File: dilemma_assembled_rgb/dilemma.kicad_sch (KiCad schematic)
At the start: 149 parts, among them J1 USB_C_Receptacle_USB2.0, J102 Serial, J105 Conn_01x04_Female, J113 Cirque, J2 Conn_01x03_Female, J5 Conn_01x02, SW1 SW_Push, SW101 SW_Push, SW102 SW_Push, SW103 SW_Push, SW104 SW_Push, SW105 SW_Push, SW106 SW_Push, SW107 SW_Push, SW108 SW_Push, SW109 SW_Push, SW110 SW_SPST, SW112 SW_Push, SW113 SW_Push, SW114 SW_Push, SW115 SW_Push, SW116 SW_Push, SW117 SW_Push, SW118 SW_Push, SW119 SW_Push, SW2 SW_Push, SW3001 SW_Push, SW3002 RotaryEncoder_Switch, U1 RP2040, U2 GD25Q80CEIGR, U3 XC6210B332MR-G, U4 USBLC6-2P6, Y1 Crystal_GND24

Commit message: edge cuts
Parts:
- D10, D11, D12, D13, D14, D15, D16, D17, D18, D19, D20, D21, D22, D23, D24, D25, D26, D27, D28, D29, D3, D4, D5, D6, D7, D8, D9: footprint 0xB2_drawings:LED_SK6805-EC15_1.5x1.5mm_P0.6mm_handsolder(1) -> 0xB2_drawings:LED_SK6805-EC15_hole
- D101, D102, D103, D104, D105, D106, D107, D108, D109, D110, D111, D112, D113, D114, D115, D116, D117, D3001: footprint local-libraries:D_1206_handsolder_reversible -> local-libraries:D_1206_handsolder_reversible_hole

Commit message: holes
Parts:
- H101, H102, H104: footprint local-libraries:MountingHole_3mm_Pad_Via -> local-libraries:MountingHole_3mm_Pad_hole
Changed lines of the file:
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@@
       (effects (font (size 1.27 1.27)) (justify left))
     )
-    (property "Footprint" "local-libraries:MountingHole_3mm_Pad_Via" (id 2) (at 184.15 176.53 0)
+    (property "Footprint" "local-libraries:MountingHole_3mm_Pad_hole" (id 2) (at 184.15 176.53 0)
       (effects (font (size 1.27 1.27)) hide)
     )
@@
       (effects (font (size 1.27 1.27)) (justify left))
     )
-    (property "Footprint" "local-libraries:MountingHole_3mm_Pad_Via" (id 2) (at 190.5 176.53 0)
+    (property "Footprint" "local-libraries:MountingHole_3mm_Pad_hole" (id 2) (at 190.5 176.53 0)
       (effects (font (size 1.27 1.27)) hide)
     )
@@
       (effects (font (size 1.27 1.27)) (justify left))
     )
-    (property "Footprint" "local-libraries:MountingHole_3mm_Pad_Via" (id 2) (at 209.55 176.53 0)
+    (property "Footprint" "local-libraries:MountingHole_3mm_Pad_hole" (id 2) (at 209.55 176.53 0)
       (effects (font (size 1.27 1.27)) hide)
     )
@@
     )
     (path "/2f4248fc-bac1-4746-8fce-b7d7e338527c"
-      (reference "H101") (unit 1) (value "M4") (footprint "local-libraries:MountingHole_3mm_Pad_Via")
+      (reference "H101") (unit 1) (value "M4") (footprint "local-libraries:MountingHole_3mm_Pad_hole")
     )
     (path "/9cb3ab70-f859-494a-87ac-434fbc66c33e"
-      (reference "H102") (unit 1) (value "M4") (footprint "local-libraries:MountingHole_3mm_Pad_Via")
+      (reference "H102") (unit 1) (value "M4") (footprint "local-libraries:MountingHole_3mm_Pad_hole")
     )
     (path "/6e8fbc4a-2a66-4de2-9627-0a21b2e2f627"
@@
     )
     (path "/b3d2b3b2-eee3-4354-96ae-35ebc3a7e3fd"
-      (reference "H104") (unit 1) (value "M4") (footprint "local-libraries:MountingHole_3mm_Pad_Via")
+      (reference "H104") (unit 1) (value "M4") (footprint "local-libraries:MountingHole_3mm_Pad_hole")
     )
     (path "/f149694e-4336-45f7-8a0b-aed91118ad18"

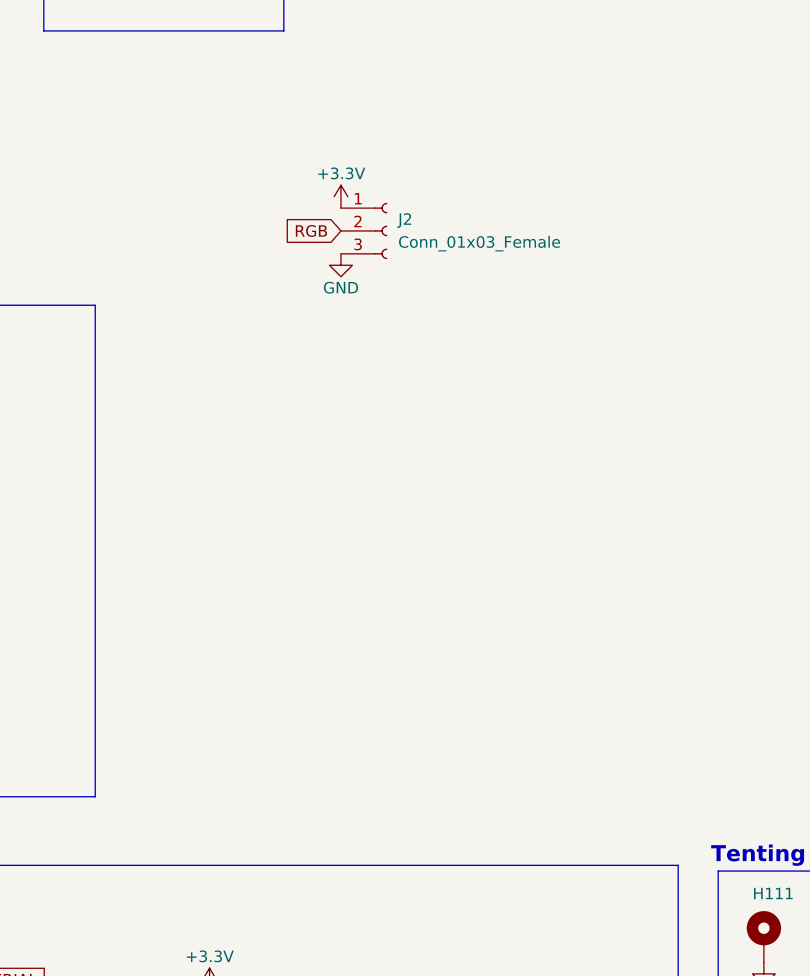
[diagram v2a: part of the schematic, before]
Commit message: switch rgb to smd connectors
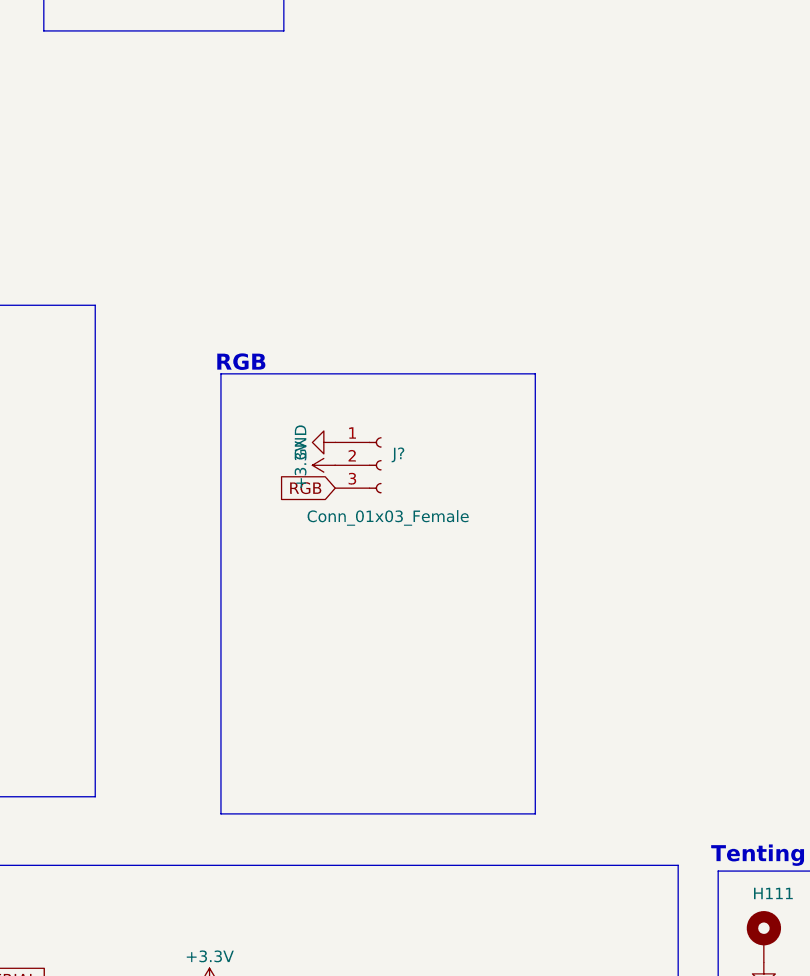
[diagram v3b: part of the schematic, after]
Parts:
- removed J2: Conn_01x03_Female, Connector_PinHeader_2.54mm:PinHeader_1x03_P2.54mm_Vertical, symbol Connector:Conn_01x03_Female
- added J?: Conn_01x03_Female, local-libraries:PinHeader_1x03_P2.54mm_Vertical_smd, symbol Connector:Conn_01x03_Female
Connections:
- net +3V3: now also J?.2 (Pin_2)
- net GND: now also J?.1 (Pin_1)
- net RGB: now also J?.3 (Pin_3)
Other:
- note added: "RGB"
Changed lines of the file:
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@@
     (stroke (width 0) (type default) (color 0 0 0 0))
   )
+  (polyline (pts (xy 293.37 111.76) (xy 328.295 111.76))
+    (stroke (width 0) (type default) (color 0 0 0 0))
+  )
   (wire (pts (xy 267.97 137.16) (xy 256.54 137.16))
     (stroke (width 0) (type default) (color 0 0 0 0))
@@
     (stroke (width 0) (type default) (color 0 0 0 0))
   )
+  (polyline (pts (xy 328.295 111.76) (xy 328.295 160.655))
+    (stroke (width 0) (type default) (color 0 0 0 0))
+  )
   (wire (pts (xy 139.7 175.26) (xy 148.59 175.26))
     (stroke (width 0) (type default) (color 0 0 0 0))
@@
     (stroke (width 0) (type default) (color 0 0 0 0))
   )
+  (polyline (pts (xy 328.295 160.655) (xy 293.37 160.655))
+    (stroke (width 0) (type default) (color 0 0 0 0))
+  )
   (wire (pts (xy 33.02 215.9) (xy 44.45 215.9))
     (stroke (width 0) (type default) (color 0 0 0 0))
@@
     (stroke (width 0) (type default) (color 0 0 0 0))
   )
+  (polyline (pts (xy 293.37 111.76) (xy 293.37 160.655))
+    (stroke (width 0) (type default) (color 0 0 0 0))
+  )
   (wire (pts (xy 111.76 81.28) (xy 116.84 81.28))
     (stroke (width 0) (type default) (color 0 0 0 0))
@@
     (effects (font (size 1.778 1.778) (thickness 0.3556) bold) (justify left bottom))
   )
+  (text "RGB" (at 292.735 111.76 0)
+    (effects (font (size 1.778 1.778) (thickness 0.3556) bold) (justify left bottom))
+  )
   (text "MCU" (at 86.36 20.32 0)
     (effects (font (size 1.778 1.778) (thickness 0.3556) bold) (justify left bottom))
@@
     )
   )
+  (global_label "RGB" (shape input) (at 306.07 124.46 180)
+    (effects (font (size 1.27 1.27)) (justify right))
+    (property "Intersheet References" "${INTERSHEET_REFS}" (id 0) (at 218.44 57.15 0)
+      (effects (font (size 1.27 1.27)) hide)
+    )
+  )
   (global_label "SERIAL" (shape input) (at 182.88 60.96 0)
     (effects (font (size 1.27 1.27)) (justify left))
@@
     )
   )
-  (global_label "RGB" (shape input) (at 306.705 95.885 180)
-    (effects (font (size 1.27 1.27)) (justify right))
-    (property "Intersheet References" "${INTERSHEET_REFS}" (id 0) (at 219.075 28.575 0)
-      (effects (font (size 1.27 1.27)) hide)
-    )
-  )
   (global_label "M_ROW1" (shape input) (at 50.8 263.525 180)
     (effects (font (size 1.27 1.27)) (justify right))
@@
     (pin "4")
   )
-  (symbol (lib_id "power:+3.3V") (at 306.705 93.345 0) (unit 1)
-    (in_bom yes) (on_board yes)
-    (property "Reference" "#PWR0119" (id 0) (at 306.705 97.155 0)
-      (effects (font (size 1.27 1.27)) hide)
-    )
-    (property "Value" "+3.3V" (id 1) (at 306.705 89.535 0))
-    (property "Footprint" "" (id 2) (at 306.705 93.345 0)
-      (effects (font (size 1.27 1.27)) hide)
-    )
-    (property "Datasheet" "" (id 3) (at 306.705 93.345 0)
-      (effects (font (size 1.27 1.27)) hide)
-    )
-    (pin "1")
-  )
   (symbol (lib_id "sk6805-ec15:SK6805-EC15") (at 548.005 76.2 0) (unit 1)
     (in_bom yes) (on_board yes)
@@
     (pin "2")
   )
+  (symbol (lib_id "power:+3.3V") (at 306.07 121.92 90) (unit 1)
+    (in_bom yes) (on_board yes)
+    (property "Reference" "#PWR?" (id 0) (at 309.88 121.92 0)
+      (effects (font (size 1.27 1.27)) hide)
+    )
+    (property "Value" "+3.3V" (id 1) (at 302.26 121.92 0))
+    (property "Footprint" "" (id 2) (at 306.07 121.92 0)
+      (effects (font (size 1.27 1.27)) hide)
+    )
+    (property "Datasheet" "" (id 3) (at 306.07 121.92 0)
+      (effects (font (size 1.27 1.27)) hide)
+    )
+    (pin "1")
+  )
   (symbol (lib_id "Device:R") (at 120.65 81.28 90) (unit 1)
     (in_bom yes) (on_board yes)
@@
     (pin "4")
   )
+  (symbol (lib_id "power:GND") (at 306.07 119.38 270) (unit 1)
+    (in_bom yes) (on_board yes)
+    (property "Reference" "#PWR?" (id 0) (at 299.72 119.38 0)
+      (effects (font (size 1.27 1.27)) hide)
+    )
+    (property "Value" "GND" (id 1) (at 302.26 119.38 0))
+    (property "Footprint" "" (id 2) (at 306.07 119.38 0)
+      (effects (font (size 1.27 1.27)) hide)
+    )
+    (property "Datasheet" "" (id 3) (at 306.07 119.38 0)
+      (effects (font (size 1.27 1.27)) hide)
+    )
+    (pin "1")
+  )
   (symbol (lib_id "power:GND") (at 286.385 59.055 0) (unit 1)
     (in_bom yes) (on_board yes)
@@
     (pin "2")
   )
-  (symbol (lib_id "Connector:Conn_01x03_Female") (at 311.785 95.885 0) (unit 1)
-    (in_bom yes) (on_board yes) (fields_autoplaced)
-    (property "Reference" "J2" (id 0) (at 313.055 94.6149 0)
+  (symbol (lib_id "Connector:Conn_01x03_Female") (at 311.15 121.92 0) (unit 1)
+    (in_bom yes) (on_board yes)
+    (property "Reference" "J?" (id 0) (at 312.42 120.6499 0)
       (effects (font (size 1.27 1.27)) (justify left))
     )
-    (property "Value" "Conn_01x03_Female" (id 1) (at 313.055 97.1549 0)
+    (property "Value" "Conn_01x03_Female" (id 1) (at 302.895 127.635 0)
       (effects (font (size 1.27 1.27)) (justify left))
     )
-    (property "Footprint" "Connector_PinHeader_2.54mm:PinHeader_1x03_P2.54mm_Vertical" (id 2) (at 311.785 95.885 0)
+    (property "Footprint" "local-libraries:PinHeader_1x03_P2.54mm_Vertical_smd" (id 2) (at 311.15 121.92 0)
       (effects (font (size 1.27 1.27)) hide)
     )
-    (property "Datasheet" "~" (id 3) (at 311.785 95.885 0)
+    (property "Datasheet" "~" (id 3) (at 311.15 121.92 0)
       (effects (font (size 1.27 1.27)) hide)
     )
@@
     (pin "2")
   )
-  (symbol (lib_id "power:GND") (at 306.705 98.425 0) (unit 1)
-    (in_bom yes) (on_board yes)
-    (property "Reference" "#PWR0126" (id 0) (at 306.705 104.775 0)
-      (effects (font (size 1.27 1.27)) hide)
-    )
-    (property "Value" "GND" (id 1) (at 306.705 102.235 0))
-    (property "Footprint" "" (id 2) (at 306.705 98.425 0)
-      (effects (font (size 1.27 1.27)) hide)
-    )
-    (property "Datasheet" "" (id 3) (at 306.705 98.425 0)
-      (effects (font (size 1.27 1.27)) hide)
-    )
-    (pin "1")
-  )
   (symbol (lib_id "Switch:SW_Push") (at 49.53 238.76 0) (unit 1)
     (in_bom yes) (on_board yes)
@@
       (reference "#PWR0118") (unit 1) (value "+3.3V") (footprint "")
     )
-    (path "/1691e08b-544b-4ddf-b972-ee3521ec471b"
-      (reference "#PWR0119") (unit 1) (value "+3.3V") (footprint "")
-    )
     (path "/6564800d-9dea-4777-82f3-5251944a6f28"
       (reference "#PWR0120") (unit 1) (value "+3.3V") (footprint "")
@@
       (reference "#PWR0125") (unit 1) (value "GND") (footprint "")
     )
-    (path "/e5db9639-93a2-41c0-8d8c-ae0f8861c21f"
-      (reference "#PWR0126") (unit 1) (value "GND") (footprint "")
-    )
     (path "/adc37c51-420c-4f8e-8736-19b6549831a9"
       (reference "#PWR0128") (unit 1) (value "GND") (footprint "")
@@
       (reference "#PWR0131") (unit 1) (value "GND") (footprint "")
     )
+    (path "/312bb836-549f-41e7-9e03-466341a7fc0a"
+      (reference "#PWR?") (unit 1) (value "+3.3V") (footprint "")
+    )
+    (path "/461ea6a6-1c8c-4a40-93fd-fe807bf8de70"
+      (reference "#PWR?") (unit 1) (value "GND") (footprint "")
+    )
     (path "/4a21e78b-0ab0-4b88-8132-9b174e045719"
       (reference "C1") (unit 1) (value "1µ") (footprint "Capacitor_SMD:C_0603_1608Metric")
@@
       (reference "J1") (unit 1) (value "USB_C_Receptacle_USB2.0") (footprint "0xLib_USB_Type-C:USB_C_Receptacle_HRO_TYPE-C-31-M-13B")
     )
-    (path "/b6253210-91e7-4539-af70-27d4e34f74cd"
-      (reference "J2") (unit 1) (value "Conn_01x03_Female") (footprint "Connector_PinHeader_2.54mm:PinHeader_1x03_P2.54mm_Vertical")
-    )
     (path "/06b6e523-10ae-4799-8871-3c7a3a700ad9"
       (reference "J5") (unit 1) (value "Conn_01x02") (footprint "Connector_PinHeader_1.27mm:PinHeader_1x02_P1.27mm_Vertical")
@@
       (reference "J113") (unit 1) (value "Cirque") (footprint "local-libraries:FPC-SMD_FPC05012-09200-.5mm")
     )
+    (path "/b73c8aa6-04a5-47a3-a2ee-6cc8eb977a8a"
+      (reference "J?") (unit 1) (value "Conn_01x03_Female") (footprint "local-libraries:PinHeader_1x03_P2.54mm_Vertical_smd")
+    )
     (path "/66096f4f-c798-4425-8537-e7adeb21bec3"

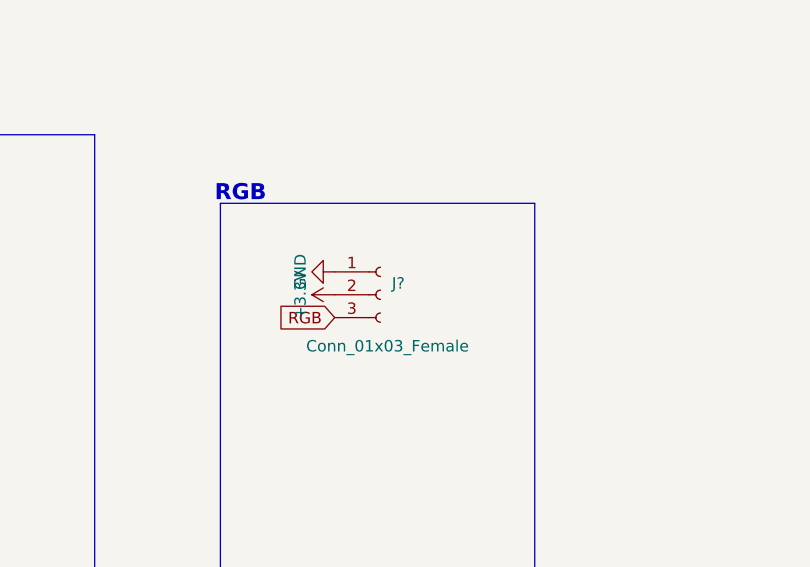
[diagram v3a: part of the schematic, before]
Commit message: flip debug headers
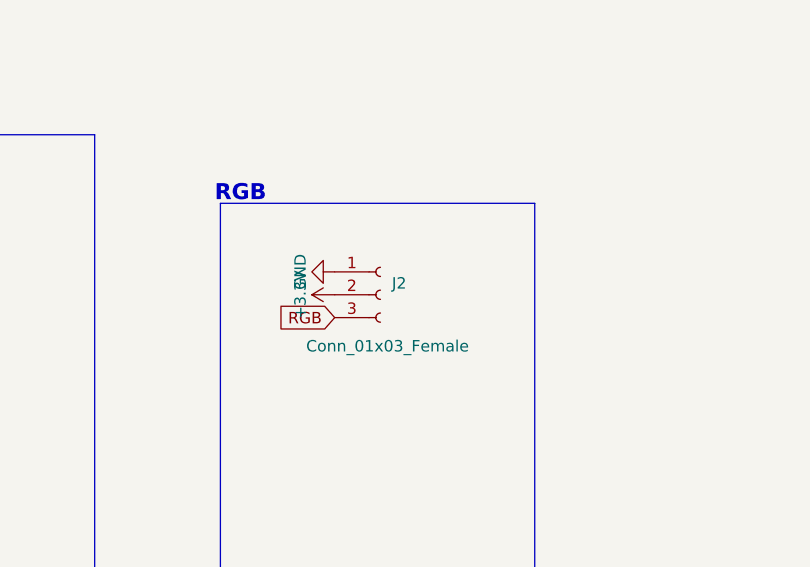
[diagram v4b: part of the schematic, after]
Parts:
- gave numbers to parts that had none: 1
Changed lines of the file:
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@@
   (symbol (lib_id "power:+3.3V") (at 306.07 121.92 90) (unit 1)
     (in_bom yes) (on_board yes)
-    (property "Reference" "#PWR?" (id 0) (at 309.88 121.92 0)
+    (property "Reference" "#PWR034" (id 0) (at 309.88 121.92 0)
       (effects (font (size 1.27 1.27)) hide)
     )
@@
   (symbol (lib_id "power:GND") (at 306.07 119.38 270) (unit 1)
     (in_bom yes) (on_board yes)
-    (property "Reference" "#PWR?" (id 0) (at 299.72 119.38 0)
+    (property "Reference" "#PWR033" (id 0) (at 299.72 119.38 0)
       (effects (font (size 1.27 1.27)) hide)
     )
@@
   (symbol (lib_id "Connector:Conn_01x03_Female") (at 311.15 121.92 0) (unit 1)
     (in_bom yes) (on_board yes)
-    (property "Reference" "J?" (id 0) (at 312.42 120.6499 0)
+    (property "Reference" "J2" (id 0) (at 312.42 120.6499 0)
       (effects (font (size 1.27 1.27)) (justify left))
     )
@@
       (reference "#PWR032") (unit 1) (value "GND") (footprint "")
     )
+    (path "/461ea6a6-1c8c-4a40-93fd-fe807bf8de70"
+      (reference "#PWR033") (unit 1) (value "GND") (footprint "")
+    )
+    (path "/312bb836-549f-41e7-9e03-466341a7fc0a"
+      (reference "#PWR034") (unit 1) (value "+3.3V") (footprint "")
+    )
     (path "/da1644f7-6b59-4f28-b4bd-963f2f055bce"
       (reference "#PWR0101") (unit 1) (value "GND") (footprint "")
@@
       (reference "#PWR0131") (unit 1) (value "GND") (footprint "")
     )
-    (path "/312bb836-549f-41e7-9e03-466341a7fc0a"
-      (reference "#PWR?") (unit 1) (value "+3.3V") (footprint "")
-    )
-    (path "/461ea6a6-1c8c-4a40-93fd-fe807bf8de70"
-      (reference "#PWR?") (unit 1) (value "GND") (footprint "")
-    )
     (path "/4a21e78b-0ab0-4b88-8132-9b174e045719"
       (reference "C1") (unit 1) (value "1µ") (footprint "Capacitor_SMD:C_0603_1608Metric")
@@
       (reference "J1") (unit 1) (value "USB_C_Receptacle_USB2.0") (footprint "0xLib_USB_Type-C:USB_C_Receptacle_HRO_TYPE-C-31-M-13B")
     )
+    (path "/b73c8aa6-04a5-47a3-a2ee-6cc8eb977a8a"
+      (reference "J2") (unit 1) (value "Conn_01x03_Female") (footprint "local-libraries:PinHeader_1x03_P2.54mm_Vertical_smd")
+    )
     (path "/06b6e523-10ae-4799-8871-3c7a3a700ad9"
       (reference "J5") (unit 1) (value "Conn_01x02") (footprint "Connector_PinHeader_1.27mm:PinHeader_1x02_P1.27mm_Vertical")
@@
       (reference "J113") (unit 1) (value "Cirque") (footprint "local-libraries:FPC-SMD_FPC05012-09200-.5mm")
     )
-    (path "/b73c8aa6-04a5-47a3-a2ee-6cc8eb977a8a"
-      (reference "J?") (unit 1) (value "Conn_01x03_Female") (footprint "local-libraries:PinHeader_1x03_P2.54mm_Vertical_smd")
-    )
     (path "/66096f4f-c798-4425-8537-e7adeb21bec3"

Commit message: cleanup
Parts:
- removed D101, D102, D103, D104, D105, D106, D107, D108, D109, D110, D111, D112, D113, D114, D115, D116, D117, D3001: D, local-libraries:D_1206_handsolder_reversible_hole, symbol Device:D
- removed D47, D48, D49, D50, D51, D52, D53, D54, D55, D56: SK6805-EC15, local-libraries:LED_SK6805-EC15_withSwitch, symbol sk6805-ec15:SK6805-EC15
- removed SW101, SW102, SW103, SW104, SW105, SW106, SW107, SW108, SW109, SW112, SW113, SW114, SW115, SW116, SW117, SW118, SW119, SW3001: SW_Push, local-libraries:SW_MX_choc, symbol Switch:SW_Push
- SW3002: footprint local-libraries:RotaryEncoder_Alps_EC11E-Switch_Vertical_H20mm_roundholes -> local-libraries:RotaryEncoder_Alps_EC11E-Switch_Vertical_H20mm_holes
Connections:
- net GND: no longer SW3002.C
- net M_ROW1: no longer SW3002.S2
- net ENC_PIN1: no longer names the net of SW3002.B
- net ENC_PIN2: no longer names the net of SW3002.A
- net encoder_diode: no longer names the net of SW3002.S1
- no-connect marks 20 -> 25
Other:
- note removed: "Diodes and switches - plate"
- note removed: "Diodes and switches - thumb cluster"
- moved on the sheet: SW3002

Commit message: cleanup
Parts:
- removed D10, D13, D14, D17, D20, D23, D26, D29, D5, D6, D9: SK6805-EC15, 0xB2_drawings:LED_SK6805-EC15_hole, symbol sk6805-ec15:SK6805-EC15
- D1: symbol Device:LED -> sk6805-ec15:SK6805-hole
- D11, D12, D15, D16, D18, D19: value SK6805-EC15 -> NA_SK6805-hole; symbol sk6805-ec15:SK6805-EC15 -> sk6805-ec15:SK6805-hole
- D21, D22, D24, D25, D27, D28, D3, D4, D7, D8: value SK6805-EC15 -> NA_SK6805-hole; footprint 0xB2_drawings:LED_SK6805-EC15_hole -> prettylib:LED_SK6805-EC15_1.5x1.5mm_P0.6mm_handsolder; symbol sk6805-ec15:SK6805-EC15 -> sk6805-ec15:SK6805-hole
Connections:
- net +3V3: no longer D11.2 (VDD), D12.2 (VDD), D15.2 (VDD), D16.2 (VDD), D18.2 (VDD), D19.2 (VDD), D21.2 (VDD), D22.2 (VDD), D24.2 (VDD), D25.2 (VDD), D27.2 (VDD), D28.2 (VDD), D3.2 (VDD), D4.2 (VDD), D7.2 (VDD), D8.2 (VDD)
- net GND: no longer D11.4 (GND), D12.4 (GND), D15.4 (GND), D16.4 (GND), D18.4 (GND), D19.4 (GND), D21.4 (GND), D22.4 (GND), D24.4 (GND), D25.4 (GND), D27.4 (GND), D28.4 (GND), D3.4 (GND), D4.4 (GND), D7.4 (GND), D8.4 (GND)
- net LED: no longer D1.2 (A)
- net RGB: now also D30.1 (DIN)
- net UNDER_RGB: no longer D3.1 (DIN), D30.1 (DIN)
- net at R1.2: no longer D1.1 (K)
- no-connect marks 25 -> 24
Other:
- note added: "holes for underglow rgb"
- note added: "per key rgb"

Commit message: cleanup
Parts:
- added D47: SK6805-EC15, local-libraries:LED_SK6805-EC15_withSwitch, symbol sk6805-ec15:SK6805-EC15
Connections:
- net +3V3: now also D47.2 (VDD)
- net GND: now also D47.4 (GND)
- net at D36.3 (DOUT): now also D47.1 (DIN); no longer D37.1 (DIN)
- new net: D37.1 (DIN), D47.3 (DOUT)
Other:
- moved on the sheet: D30, D31, D32, D33, D34, D35, D36, D37, D38, D39, D40, D41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
